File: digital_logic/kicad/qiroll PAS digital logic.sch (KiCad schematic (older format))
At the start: 40 parts, among them J1 led_sw1, J2 mode_thr_batt, J3 pas_sense, J4 brk_sense, J5 jumper, U1 14538, U2 4023, U3 4027, U4 14538, U5 L7805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

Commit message: add brake sensor pulldown, incomplete BOM
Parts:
- added R11: 10k, Resistor_SMD:R_0603_1608Metric, symbol Device:R
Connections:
- net BRK: now also R11.1
- net GND: now also R11.2
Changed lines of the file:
@@
 	-1   0    0    1
 $EndComp
-Text GLabel 7050 900  3    50   Input ~ 0
+Text GLabel 7050 1050 3    50   Input ~ 0
 BRK
 Text GLabel 5950 3400 0    50   Input ~ 0
@@
 Wire Wire Line
 	6250 1650 6250 1500
-Wire Wire Line
-	6150 1750 6700 1750
 Wire Wire Line
 	5900 2300 5950 2300
@@
 Wire Wire Line
 	7700 1750 7850 1750
-Wire Wire Line
-	7400 1750 6700 1750
-Connection ~ 6700 1750
 $Comp
 L 4xxx:14538 U1
@@
 Wire Wire Line
 	8000 1750 8100 1750
+Wire Wire Line
+	6150 1750 7400 1750
+Wire Wire Line
+	7050 1050 7050 1000
+Wire Wire Line
+	7050 1000 7250 1000
+Connection ~ 7050 1000
+Wire Wire Line
+	7050 1000 7050 900
+$Comp
+L Device:R R11
+U 1 1 60E0D46A
+P 7400 1000
+F 0 "R11" V 7200 1000 50  0000 C CNN
+F 1 "10k" V 7300 1000 50  0000 C CNN
+F 2 "Resistor_SMD:R_0603_1608Metric" V 7330 1000 50  0001 C CNN
+F 3 "~" H 7400 1000 50  0001 C CNN
+	1    7400 1000
+	0    -1   -1   0
+$EndComp
+$Comp
+L power:GND #PWR?
+U 1 1 60E123A7
+P 7550 1000
+F 0 "#PWR?" H 7550 750 50  0001 C CNN
+F 1 "GND" V 7555 872 50  0000 R CNN
+F 2 "" H 7550 1000 50  0001 C CNN
+F 3 "" H 7550 1000 50  0001 C CNN
+	1    7550 1000
+	0    -1   -1   0
+$EndComp
 $EndSCHEMATC

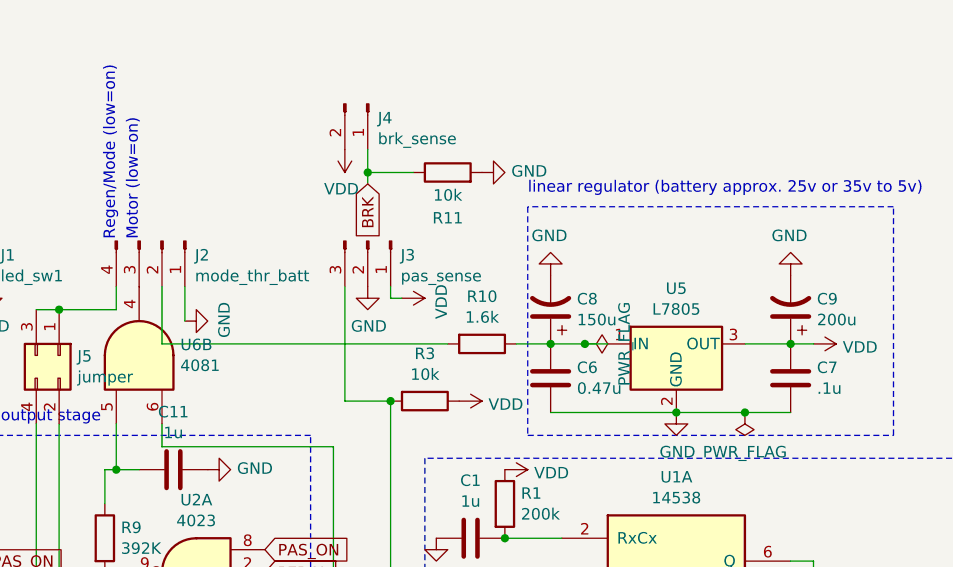
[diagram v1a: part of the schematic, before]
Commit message: add ptc and protection diode for voltage reg
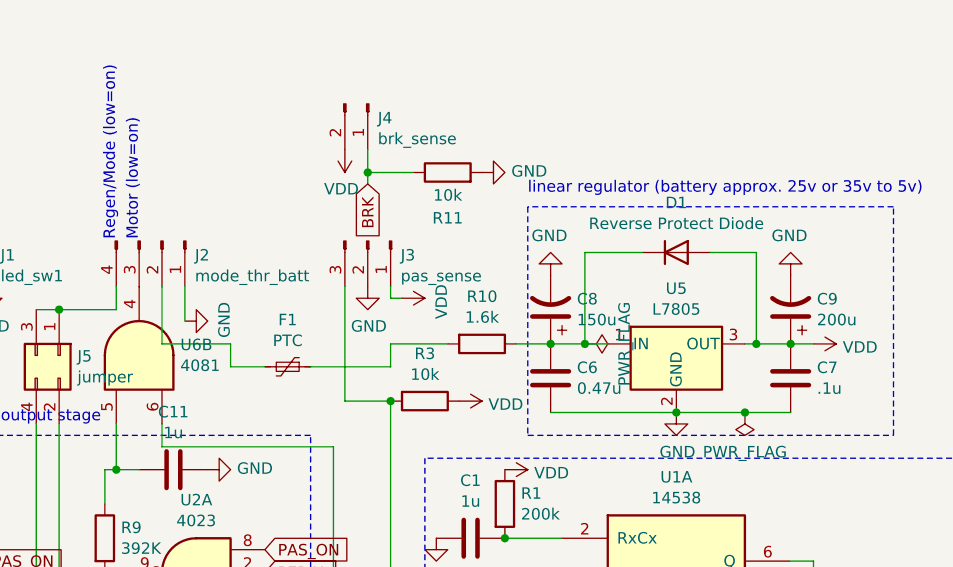
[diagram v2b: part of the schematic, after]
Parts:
- added D1: Reverse Protect Diode, Diode_SMD:D_MiniMELF, symbol Device:D
- added F1: PTC, Fuse:Fuse_1206_3216Metric, symbol Device:Polyfuse_Small
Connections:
- net VCC: now also D1.2 (A)
- net at C6.1, C8.1, R10.1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: now also D1.1 (K)
- net at J2.2 (Pin_2): now also F1.2; no longer R10.2
- new net: F1.1, R10.2
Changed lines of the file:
@@
 $EndComp
 Wire Wire Line
-	8700 1750 8900 1750
+	8700 1750 8750 1750
 $Comp
 L power:GND #PWR0144
@@
 	8000 1750 8100 1750
 Wire Wire Line
-	6150 1750 7400 1750
-Wire Wire Line
 	7050 1050 7050 1000
 Wire Wire Line
@@
 $EndComp
 $Comp
-L power:GND #PWR?
+L power:GND #PWR0165
 U 1 1 60E123A7
 P 7550 1000
-F 0 "#PWR?" H 7550 750 50  0001 C CNN
+F 0 "#PWR0165" H 7550 750 50  0001 C CNN
 F 1 "GND" V 7555 872 50  0000 R CNN
 F 2 "" H 7550 1000 50  0001 C CNN
@@
 	0    -1   -1   0
 $EndComp
+$Comp
+L Device:Polyfuse_Small F1
+U 1 1 60E03DF4
+P 6700 1850
+F 0 "F1" V 6495 1850 50  0000 C CNN
+F 1 "PTC" V 6586 1850 50  0000 C CNN
+F 2 "Fuse:Fuse_1206_3216Metric" H 6750 1650 50  0001 L CNN
+F 3 "https://www.digikey.com/en/products/detail/bel-fuse-inc/0ZCJ0012FF2E/4156129~" H 6700 1850 50  0001 C CNN
+	1    6700 1850
+	0    1    1    0
+$EndComp
+Wire Wire Line
+	7150 1750 7400 1750
+Wire Wire Line
+	7150 1750 7150 1850
+Wire Wire Line
+	7150 1850 6800 1850
+Wire Wire Line
+	6600 1850 6450 1850
+Wire Wire Line
+	6450 1850 6450 1750
+Wire Wire Line
+	6450 1750 6150 1750
+Wire Wire Line
+	8000 1750 8000 1350
+Wire Wire Line
+	8000 1350 8250 1350
+$Comp
+L Device:D D1
+U 1 1 60E52D25
+P 8400 1350
+F 0 "D1" H 8400 1567 50  0000 C CNN
+F 1 "Reverse Protect Diode" H 8400 1476 50  0000 C CNN
+F 2 "Diode_SMD:D_MiniMELF" H 8400 1350 50  0001 C CNN
+F 3 "https://www.digikey.com/en/products/detail/vishay-general-semiconductor-diodes-division/LL4150GS18/4810537" H 8400 1350 50  0001 C CNN
+	1    8400 1350
+	1    0    0    -1
+$EndComp
+Wire Wire Line
+	8550 1350 8750 1350
+Wire Wire Line
+	8750 1350 8750 1750
+Connection ~ 8750 1750
+Wire Wire Line
+	8750 1750 8900 1750
 $EndSCHEMATC

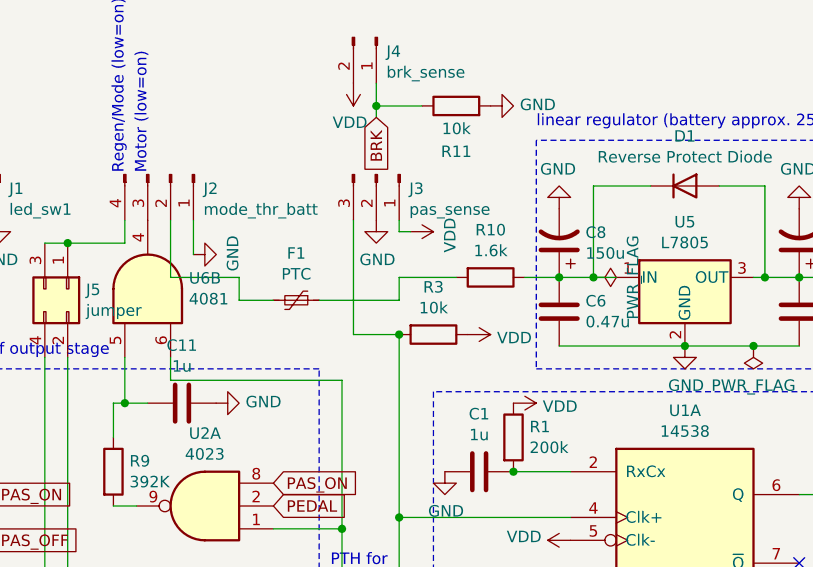
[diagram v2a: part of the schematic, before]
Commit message: revised pcb w/ ptc, protection diode, revised c11 value
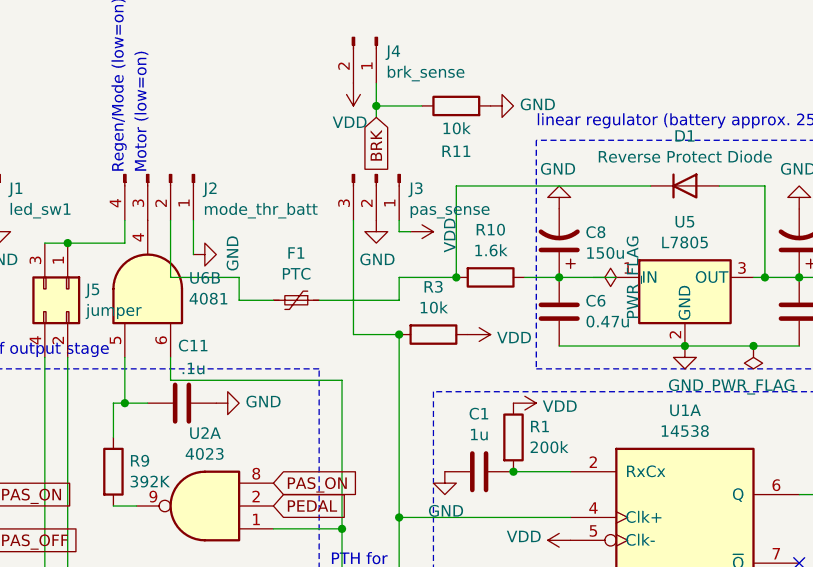
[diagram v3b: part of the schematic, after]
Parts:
- C11: value 1u -> .1u
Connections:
- net at C6.1, C8.1, R10.1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: no longer D1.1 (K)
- net at F1.1, R10.2: now also D1.1 (K)
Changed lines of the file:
@@
 Wire Wire Line
 	7150 1550 7150 1500
-Wire Wire Line
-	7850 1750 8000 1750
 $Comp
 L power:PWR_FLAG #FLG0101
@@
 U 1 1 60E015DA
 P 6200 2300
-F 0 "C11" V 5948 2300 50  0000 C CNN
-F 1 "1u" V 6039 2300 50  0000 C CNN
+F 0 "C11" V 5950 2350 50  0000 C CNN
+F 1 ".1u" V 6050 2350 50  0000 C CNN
 F 2 "Capacitor_SMD:C_0603_1608Metric" H 6238 2150 50  0001 C CNN
 F 3 "https://www.digikey.com/en/products/detail/tdk-corporation/C1608X7R1C105K080AC/634399" H 6200 2300 50  0001 C CNN
@@
 	0    1    1    0
 $EndComp
-Connection ~ 8000 1750
-Wire Wire Line
-	8000 1750 8100 1750
 Wire Wire Line
 	7050 1050 7050 1000
@@
 Wire Wire Line
 	6450 1750 6150 1750
-Wire Wire Line
-	8000 1750 8000 1350
-Wire Wire Line
-	8000 1350 8250 1350
 $Comp
 L Device:D D1
@@
 Wire Wire Line
 	8750 1750 8900 1750
+Wire Wire Line
+	7850 1750 8100 1750
+Wire Wire Line
+	7400 1350 7400 1750
+Wire Wire Line
+	7400 1350 8250 1350
+Connection ~ 7400 1750
 $EndSCHEMATC
